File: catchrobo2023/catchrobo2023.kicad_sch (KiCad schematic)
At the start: 17 parts

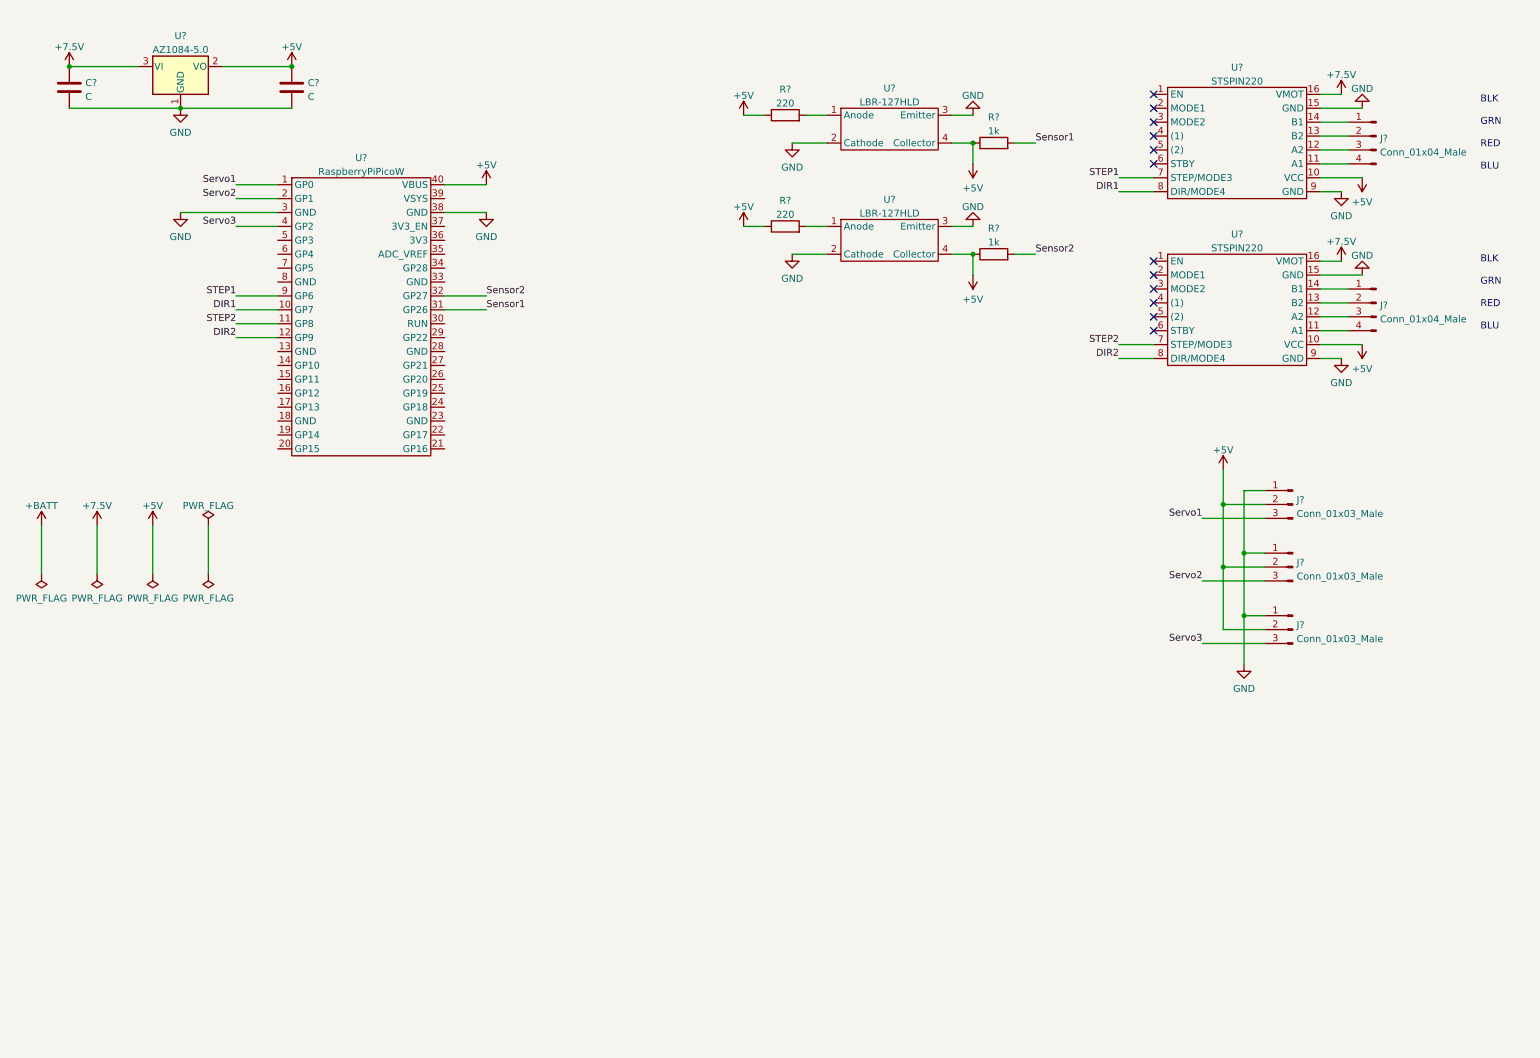
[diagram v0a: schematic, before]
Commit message: リレーまで追加
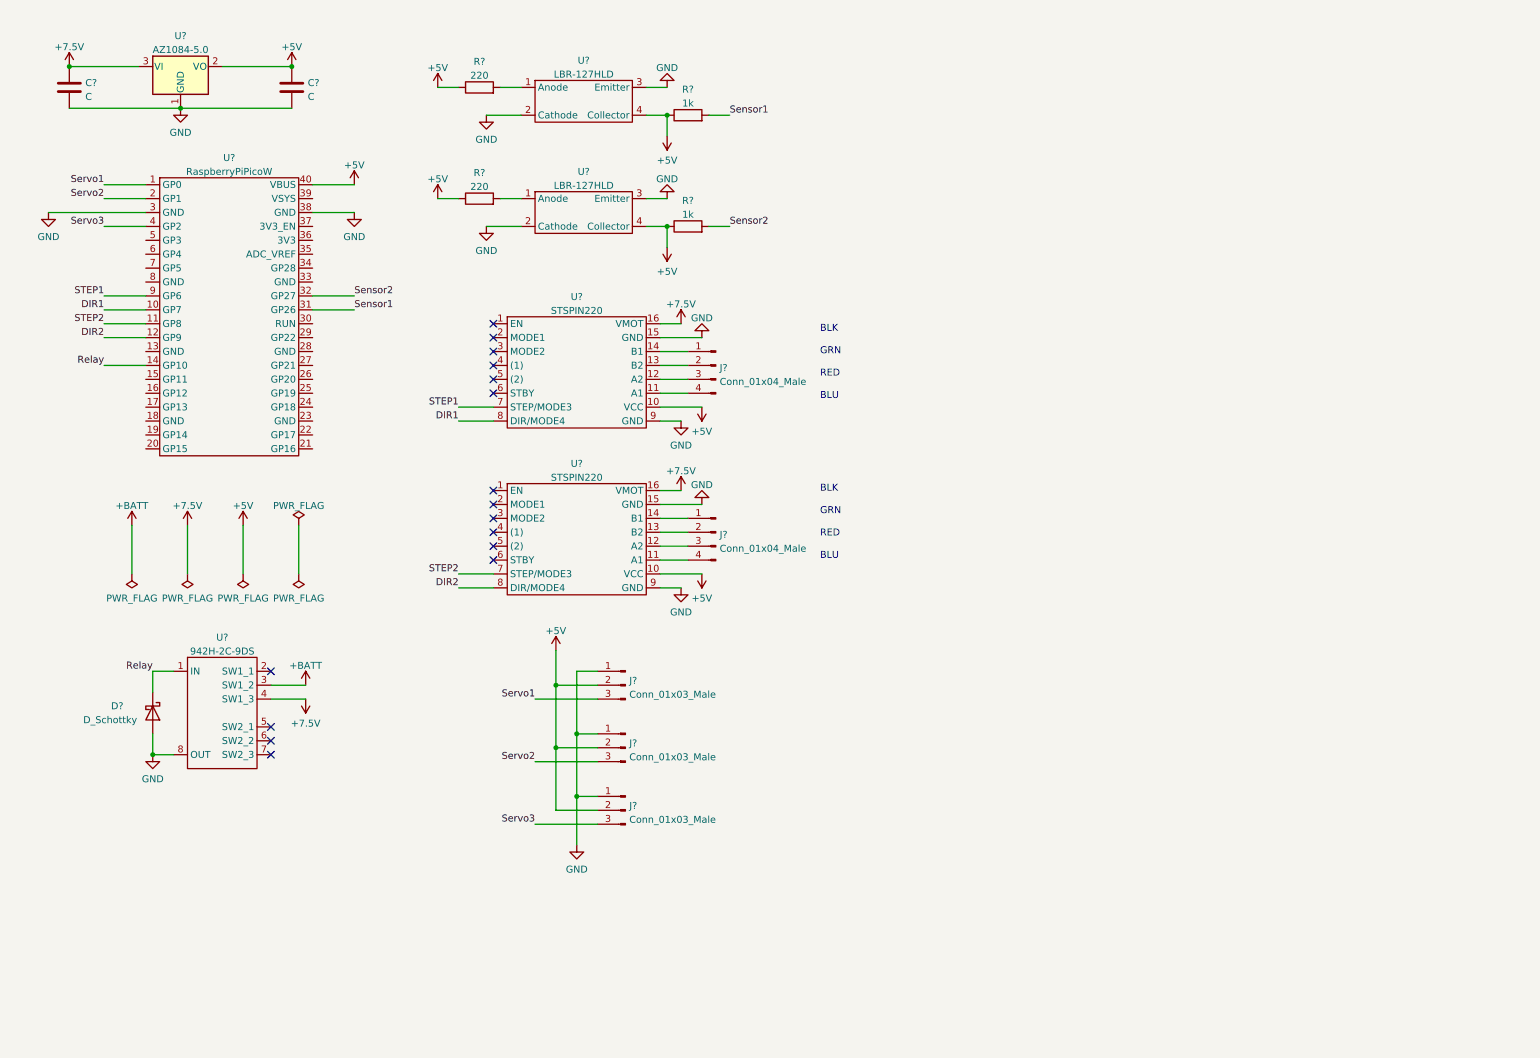
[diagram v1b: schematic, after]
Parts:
- added D?: D_Schottky, symbol Device:D_Schottky
- added U?: 942H-2C-9DS, symbol catchrobo_parts:942H-2C-9DS
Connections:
- net +7.5V: now also U?.4 (SW1_3)
- net +BATT: now also U?.3 (SW1_2)
- net GND: now also D?.2 (A), U?.8 (OUT)
- net Relay: now reaches U?.14 (GP10)
- net Relay: now also D?.1 (K), U?.1 (IN)
- no-connect marks 12 -> 16
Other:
- moved on the sheet: J?, R?, U?

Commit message: 緊急非常停止以外の回路図は完了
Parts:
- added D?: LED, symbol Device:LED
- added D?: D_Schottky, symbol Device:D_Schottky
- added R? (x2): 220, symbol Device:R
- added R? (x3): 1k, symbol Device:R
- added SW?: SW_DPDT_x2, symbol Switch:SW_DPDT_x2
- added U?: SPT15, symbol catchrobo_parts:SPT15
- added U? (x2): LBR-127HLD, symbol catchrobo_parts:LBR-127HLD
- added U?: TC74HC4052A, symbol catchrobo_parts:TC74HC4052A
- C? (x2): value C -> 100u
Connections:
- net +5V: now also D?.2 (A), R?.1, R?.1, R?.1, R?.1, U?.16 (Vcc), U?.4 (Collector), U?.4 (Collector)
- net +7.5V: now also D?.1 (K), R?.1
- net +BATT: now also SW?.2 (B); no longer U?.3 (SW1_2)
- net DIR2: now also U?.15 (GP11); no longer U?.12 (GP9)
- net GND: now also D?.1 (K), U?.2 (Cathode), U?.2 (Cathode), U?.2 (OUT), U?.3 (Emitter), U?.3 (Emitter), U?.6 (INH), U?.7 (Vee), U?.8 (GND)
- net Relay: now also U?.16 (GP12); no longer U?.14 (GP10)
- net STEP2: now also U?.14 (GP10); no longer U?.11 (GP8)
- net Sensor1: now also U?.2 (2Y); no longer U?.31 (GP26)
- net Sensor2: now also U?.4 (3Y); no longer U?.32 (GP27)
- net MultiA: now reaches U?.19 (GP14)
- net MultiA: now also U?.10 (A)
- net MultiB: now reaches U?.20 (GP15)
- net MultiB: now also U?.9 (B)
- net Sensor: now reaches U?.34 (GP28)
- net Sensor: now also U?.3 (Y-COM)
- net Speaker: now reaches U?.5 (GP3)
- net Speaker: now also U?.1 (IN)
- new net: R?.2, U?.1 (Anode) (x2)
- new net: SW?.3 (C), U?.3 (SW1_2)
- new net: D?.2 (A), R?.2
- new net Sensor0: R?.2, U?.1 (0Y)
- new net Sensor3: R?.2, U?.5 (1Y)
- no-connect marks 16 -> 47
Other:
- moved on the sheet: C?, D?, J?, R?, U?

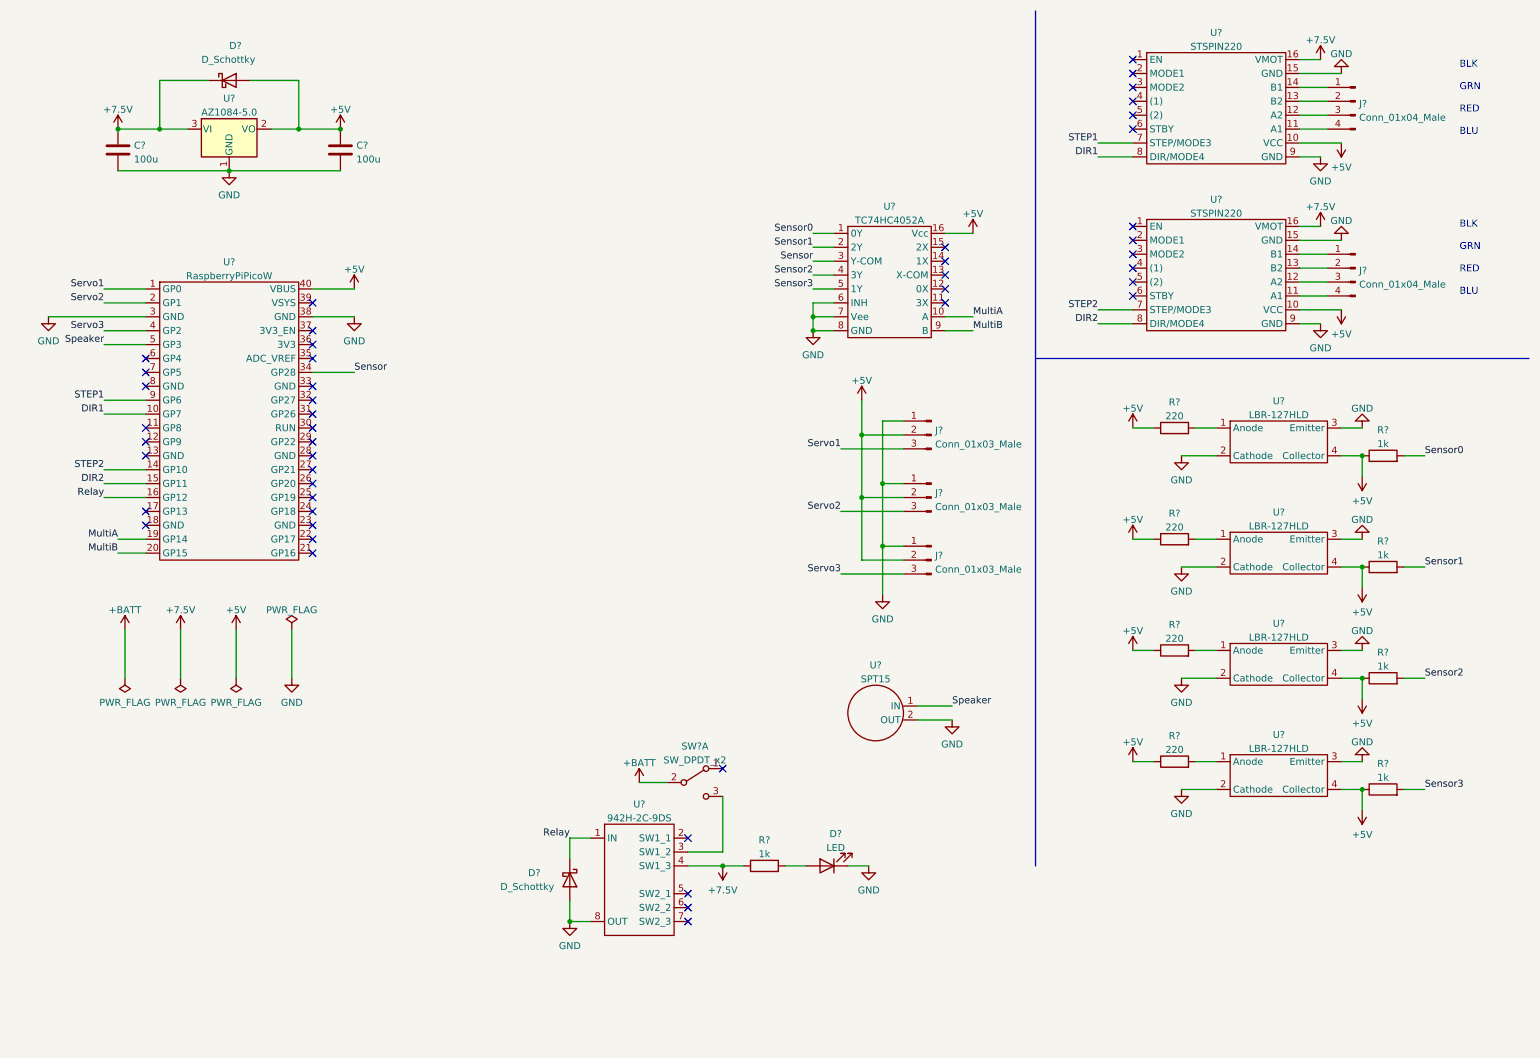
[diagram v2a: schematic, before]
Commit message: フットプリントを一部選定
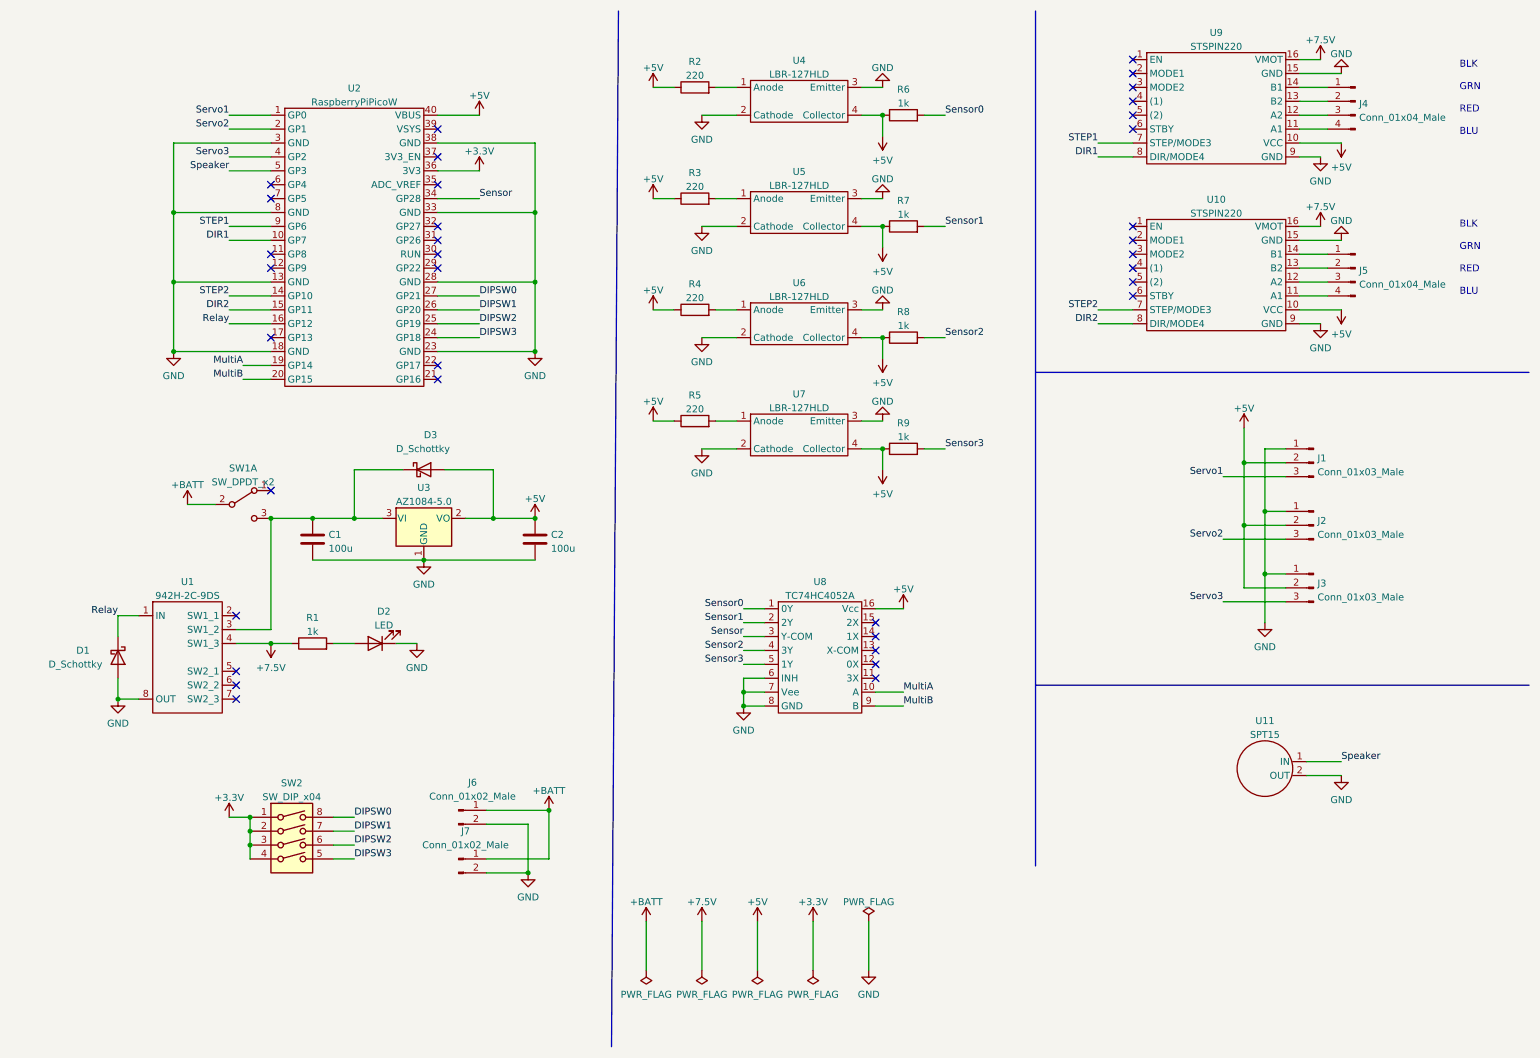
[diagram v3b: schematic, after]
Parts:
- added J6, J7: Conn_01x02_Male, Connector_JST:JST_XH_S2B-XH-A-1_1x02_P2.50mm_Horizontal, symbol Connector:Conn_01x02_Male
- added SW2: SW_DIP_x04, symbol Switch:SW_DIP_x04
- D1: renamed from D?; footprint (none) -> Diode_SMD:D_SOD-323; LCSC (none) -> C191023
- D2: renamed from D?; footprint (none) -> LED_THT:LED_D5.0mm
- J1, J2, J3: renamed from J?; footprint (none) -> Connector_JST:JST_XH_S3B-XH-A-1_1x03_P2.50mm_Horizontal
- J4, J5: renamed from J?; footprint (none) -> Connector_JST:JST_XH_S4B-XH-A-1_1x04_P2.50mm_Horizontal
- R1: renamed from R?; footprint (none) -> Resistor_SMD:R_0402_1005Metric
- R2, R3, R4, R5: renamed from R?; footprint (none) -> Resistor_SMD:R_0201_0603Metric; LCSC (none) -> C22962
- R6, R7, R8, R9: renamed from R?; footprint (none) -> Resistor_SMD:R_0402_1005Metric; LCSC (none) -> C11702
- U11, U4, U5, U6, U7: renamed from U?; footprint (none) -> Connector_JST:JST_XH_S2B-XH-A-1_1x02_P2.50mm_Horizontal
- U3: renamed from U?; footprint (none) -> Package_TO_SOT_SMD:TO-252-2
- U8: renamed from U?; footprint (none) -> Package_DIP:DIP-16_W7.62mm_Socket
- gave numbers to parts that had none: 8
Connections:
- net +7.5V: no longer C1.1, D3.1 (K), U3.3 (VI)
- net +BATT: now also J6.1 (Pin_1), J7.1 (Pin_1)
- net GND: now also U2.13 (GND), U2.18 (GND), U2.23 (GND), U2.28 (GND), U2.33 (GND), U2.8 (GND), J6.2 (Pin_2), J7.2 (Pin_2)
- net at SW1.3 (C), U1.3 (SW1_2): now also C1.1, D3.1 (K), U3.3 (VI)
- net DIPSW3: now reaches U2.24 (GP18)
- net DIPSW3: now also SW2.5
- net DIPSW2: now reaches U2.25 (GP19)
- net DIPSW2: now also SW2.6
- net DIPSW1: now reaches U2.26 (GP20)
- net DIPSW1: now also SW2.7
- net DIPSW0: now reaches U2.27 (GP21)
- net DIPSW0: now also SW2.8
- net +3.3V: now reaches U2.36 (3V3)
- net +3.3V: now also SW2.1, SW2.2, SW2.3, SW2.4
- no-connect marks 47 -> 36
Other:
- moved on the sheet: C1, C2, D1, D2, D3, J1, J2, J3, R1, R2, R3, R4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

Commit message: README追加
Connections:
- net DIPSW0: now also U2.24 (GP18); no longer U2.27 (GP21)
- net DIPSW1: now also U2.25 (GP19); no longer U2.26 (GP20)
- net DIPSW2: now also U2.26 (GP20); no longer U2.25 (GP19)
- net DIPSW3: now also U2.27 (GP21); no longer U2.24 (GP18)
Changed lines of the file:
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@@
     (effects (font (size 1.27 1.27)) (justify right bottom))
   )
-  (label "DIPSW3" (at 95.25 69.85 0)
+  (label "DIPSW0" (at 95.25 69.85 0)
     (effects (font (size 1.27 1.27)) (justify left bottom))
   )
@@
     (effects (font (size 1.27 1.27)) (justify right bottom))
   )
-  (label "DIPSW0" (at 95.25 62.23 0)
+  (label "DIPSW3" (at 95.25 62.23 0)
     (effects (font (size 1.27 1.27)) (justify left bottom))
   )
@@
     (effects (font (size 1.27 1.27)) (justify right bottom))
   )
-  (label "DIPSW2" (at 95.25 67.31 0)
+  (label "DIPSW1" (at 95.25 67.31 0)
     (effects (font (size 1.27 1.27)) (justify left bottom))
   )
@@
     (effects (font (size 1.27 1.27)) (justify right bottom))
   )
-  (label "DIPSW1" (at 95.25 64.77 0)
+  (label "DIPSW2" (at 95.25 64.77 0)
     (effects (font (size 1.27 1.27)) (justify left bottom))
   )

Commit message: フットプリントの割り当て途中②
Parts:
- C1, C2: footprint (none) -> Capacitor_THT:C_Radial_D5.0mm_H11.0mm_P2.00mm
- SW2: footprint (none) -> Package_DIP:DIP-8_W7.62mm
- U10, U9: footprint (none) -> Catchrobo_parts:STSPIN220
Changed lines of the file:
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@@
       (effects (font (size 1.27 1.27)) (justify left))
     )
-    (property "Footprint" "" (id 2) (at 65.7352 110.49 0)
+    (property "Footprint" "Capacitor_THT:C_Radial_D5.0mm_H11.0mm_P2.00mm" (id 2) (at 65.7352 110.49 0)
       (effects (font (size 1.27 1.27)) hide)
     )
@@
     (property "Reference" "U10" (id 0) (at 229.87 44.611 0))
     (property "Value" "STSPIN220" (id 1) (at 229.87 47.1479 0))
-    (property "Footprint" "" (id 2) (at 227.33 60.96 0)
+    (property "Footprint" "Catchrobo_parts:STSPIN220" (id 2) (at 227.33 60.96 0)
       (effects (font (size 1.27 1.27)) hide)
     )
@@
     (property "Reference" "U9" (id 0) (at 229.87 14.131 0))
     (property "Value" "STSPIN220" (id 1) (at 229.87 16.6679 0))
-    (property "Footprint" "" (id 2) (at 227.33 30.48 0)
+    (property "Footprint" "Catchrobo_parts:STSPIN220" (id 2) (at 227.33 30.48 0)
       (effects (font (size 1.27 1.27)) hide)
     )
@@
     (property "Reference" "SW2" (id 0) (at 60.96 151.2402 0))
     (property "Value" "SW_DIP_x04" (id 1) (at 60.96 153.7771 0))
-    (property "Footprint" "" (id 2) (at 60.96 162.56 0)
+    (property "Footprint" "Package_DIP:DIP-8_W7.62mm" (id 2) (at 60.96 162.56 0)
       (effects (font (size 1.27 1.27)) hide)
     )
@@
       (effects (font (size 1.27 1.27)) (justify left))
     )
-    (property "Footprint" "" (id 2) (at 106.3752 110.49 0)
+    (property "Footprint" "Capacitor_THT:C_Radial_D5.0mm_H11.0mm_P2.00mm" (id 2) (at 106.3752 110.49 0)
       (effects (font (size 1.27 1.27)) hide)
     )
@@
     )
     (path "/7c4cf30b-40be-4e88-b1a4-631cdeaa5354"
-      (reference "C1") (unit 1) (value "100u") (footprint "")
+      (reference "C1") (unit 1) (value "100u") (footprint "Capacitor_THT:C_Radial_D5.0mm_H11.0mm_P2.00mm")
     )
     (path "/f1ea9074-cc79-4bdc-8375-68a92f1f00cc"
-      (reference "C2") (unit 1) (value "100u") (footprint "")
+      (reference "C2") (unit 1) (value "100u") (footprint "Capacitor_THT:C_Radial_D5.0mm_H11.0mm_P2.00mm")
     )
     (path "/d9f3dddd-27ac-46e5-ae48-bafbcbf81d8c"
@@
     )
     (path "/d326836a-3a12-431e-8f05-d632472e9eb8"
-      (reference "SW2") (unit 1) (value "SW_DIP_x04") (footprint "")
+      (reference "SW2") (unit 1) (value "SW_DIP_x04") (footprint "Package_DIP:DIP-8_W7.62mm")
     )
     (path "/5ccd5fa3-a1d2-4653-a35a-1d86acd5201c"
@@
     )
     (path "/c0c1c426-32ce-4e58-ad7b-ad0f382a982b"
-      (reference "U9") (unit 1) (value "STSPIN220") (footprint "")
+      (reference "U9") (unit 1) (value "STSPIN220") (footprint "Catchrobo_parts:STSPIN220")
     )
     (path "/8edf91d6-eff2-4aec-960c-cdc9190d1f9d"
-      (reference "U10") (unit 1) (value "STSPIN220") (footprint "")
+      (reference "U10") (unit 1) (value "STSPIN220") (footprint "Catchrobo_parts:STSPIN220")
     )
     (path "/2d7e83a6-69d3-438f-a10a-517e6ac07561"
